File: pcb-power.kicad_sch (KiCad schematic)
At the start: 9 parts, among them Q1 PMOS, Q3 PMOS, Q4 PMOS, U1 LM1117MP-3.3, U2 LM1117MP-3.3

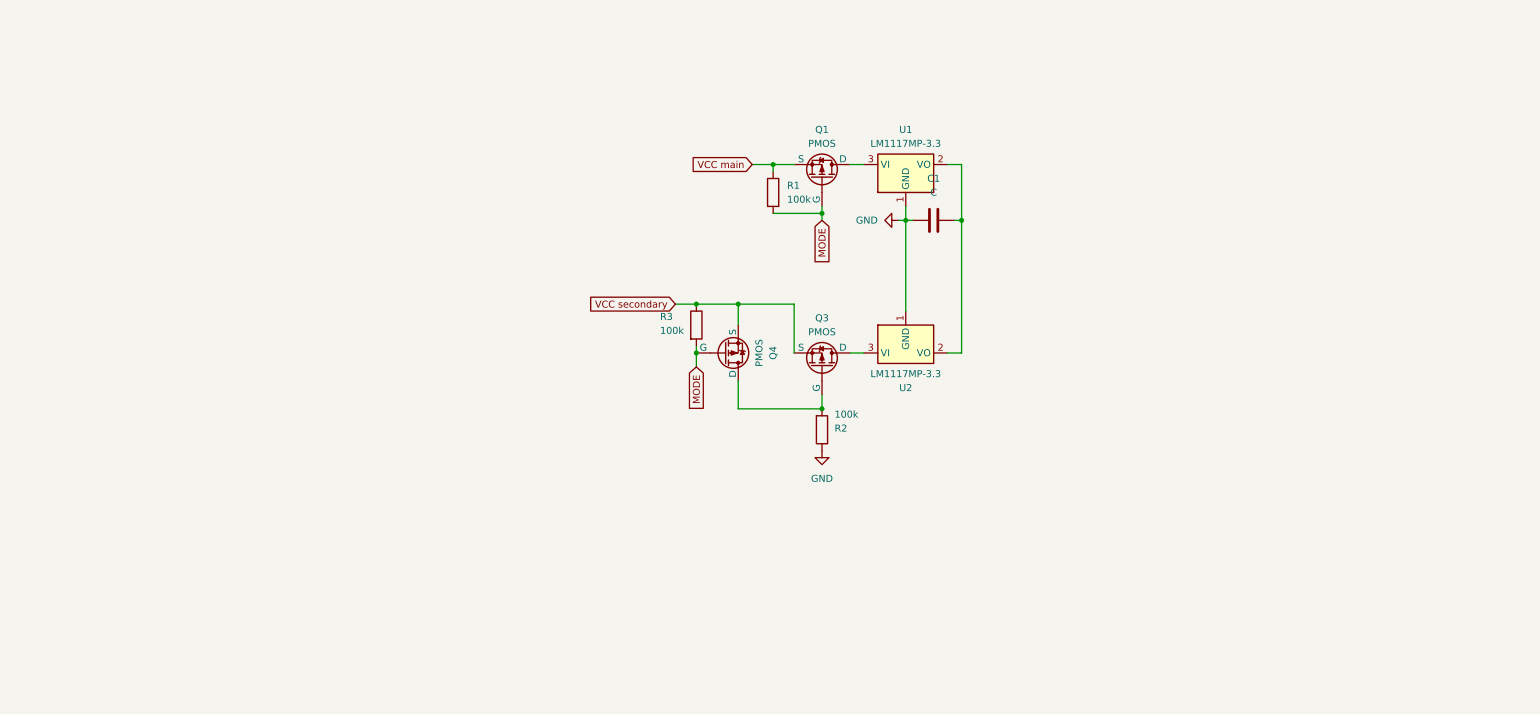
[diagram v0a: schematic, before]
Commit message: added pyro, voltage probes, signal
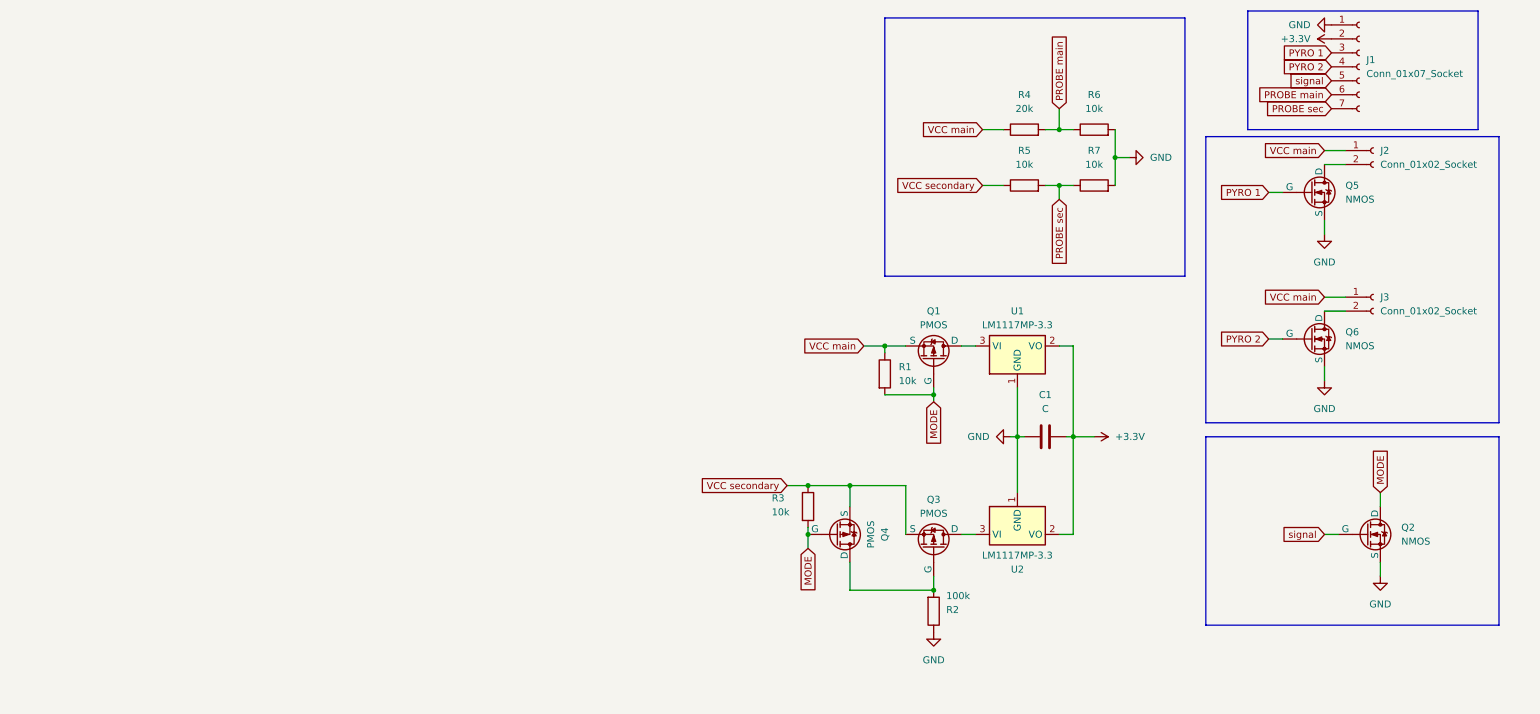
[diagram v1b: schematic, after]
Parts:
- added J1: Conn_01x07_Socket, symbol Connector:Conn_01x07_Socket
- added J2, J3: Conn_01x02_Socket, symbol Connector:Conn_01x02_Socket
- added Q2, Q5, Q6: NMOS, symbol Simulation_SPICE:NMOS
- added R4: 20k, symbol Device:R
- added R5, R6, R7: 10k, symbol Device:R
- R1, R3: value 100k -> 10k
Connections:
- net GND: now also J1.1 (Pin_1), Q2.3 (S), Q5.3 (S), Q6.3 (S), R6.2, R7.2
- net MODE: now also Q2.1 (D)
- net VCC main: now also J2.1 (Pin_1), J3.1 (Pin_1), R4.1
- net VCC secondary: now also R5.1
- net +3.3V: now reaches C1.2, U1.2 (VO), U2.2 (VO)
- net +3.3V: now also J1.2 (Pin_2)
- new net: J2.2 (Pin_2), Q5.1 (D)
- new net: J3.2 (Pin_2), Q6.1 (D)
- new net PROBE main: J1.6 (Pin_6), R4.2, R6.1
- new net PROBE sec: J1.7 (Pin_7), R5.2, R7.1
- new net PYRO 1: J1.3 (Pin_3), Q5.2 (G)
- new net PYRO 2: J1.4 (Pin_4), Q6.2 (G)
- new net signal: J1.5 (Pin_5), Q2.2 (G)
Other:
- moved on the sheet: C1, Q1, Q3, Q4, R1, R2, R3, U1, U2

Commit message: pcb design done
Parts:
- removed Q1, Q3: PMOS, symbol Simulation_SPICE:PMOS
- removed Q5, Q6: NMOS, symbol Simulation_SPICE:NMOS
- removed R1, R3: 10k, symbol Device:R
- removed R2: 100k, symbol Device:R
- removed U1, U2: LM1117MP-3.3, Package_TO_SOT_SMD:SOT-223-3_TabPin2, symbol Regulator_Linear:LM1117MP-3.3
- added R10, R8, R9: 10k, Resistor_THT:R_Axial_DIN0207_L6.3mm_D2.5mm_P10.16mm_Horizontal, symbol Device:R
- added U1, U3: LM1117DT-5.0, Package_TO_SOT_SMD:TO-252-3_TabPin2, symbol Regulator_Linear:LM1117DT-5.0
- added U2: IRF7303, Package_TO_SOT_SMD:IRF7303, symbol Transistor_FET:IRF7303
- added U4: IRF7104, Package_TO_SOT_SMD:IRF7104, symbol Transistor_FET:IRF7104
- C1: footprint (none) -> Capacitor_THT:CP_Radial_D5.0mm_P2.00mm
- J1: footprint (none) -> Connector_PinSocket_2.54mm:PinSocket_1x07_P2.54mm_Vertical
- J2, J3: footprint (none) -> ark:TerminalBlock_bornier-2_P5.08mm
- Q2: footprint (none) -> Package_TO_SOT_SMD:SOT-23
- Q4: footprint (none) -> Package_TO_SOT_SMD:TO-252-2
- R4, R5, R6, R7: footprint (none) -> Resistor_THT:R_Axial_DIN0207_L6.3mm_D2.5mm_P10.16mm_Horizontal
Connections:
- net +3.3V: now also U1.2 (VO), U3.2 (VO)
- net GND: now also R9.1, U1.1 (GND), U2.1 (S1), U2.3 (S2), U3.1 (GND)
- net MODE: now also R10.2, R8.1, U4.4 (G2)
- net PYRO 1: now also U2.2 (G1)
- net PYRO 2: now also U2.4 (G2)
- net VCC main: now also J2.2 (Pin_2), J3.2 (Pin_2), Q4.3 (S), R10.1, U4.1 (S1); no longer J2.1 (Pin_1), J3.1 (Pin_1)
- net VCC secondary: now also R8.2, U4.3 (S2); no longer Q4.3 (S)
- net at Q4.1 (D): now also R9.2, U4.2 (G1)
- new net: J2.1 (Pin_1), U2.5 (D2)
- new net: J3.1 (Pin_1), U2.6 (D1)
- new net: U3.3 (VI), U4.5 (D2)
- new net: U1.3 (VI), U4.6 (D1)
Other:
- moved on the sheet: C1, J2, J3, Q2

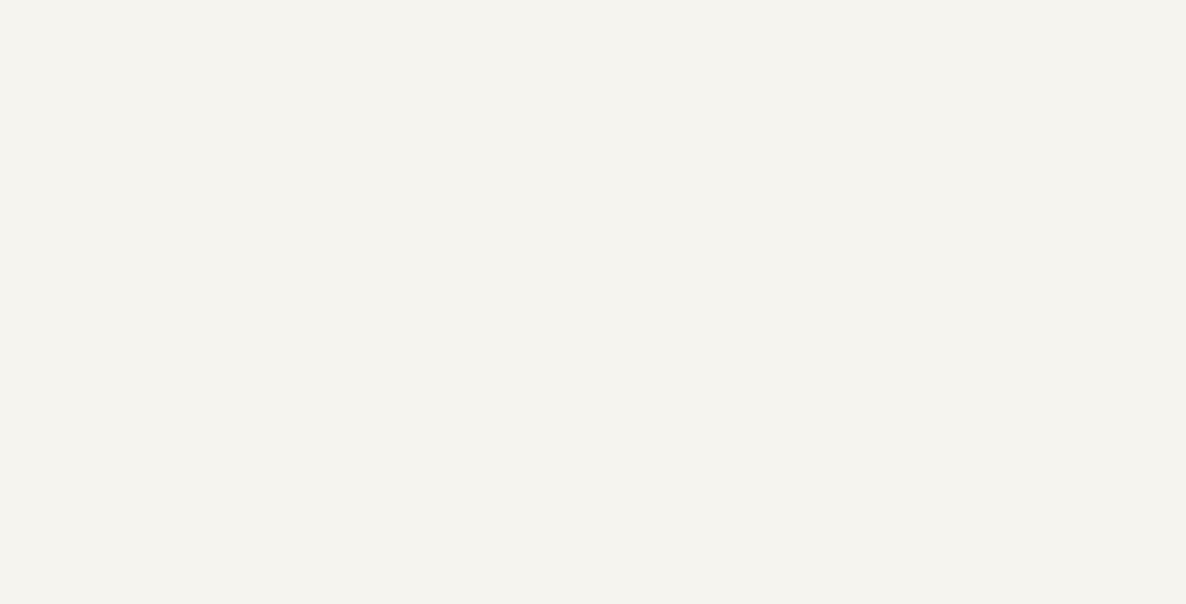
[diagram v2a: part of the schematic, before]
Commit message: added second layer for connecting batteries
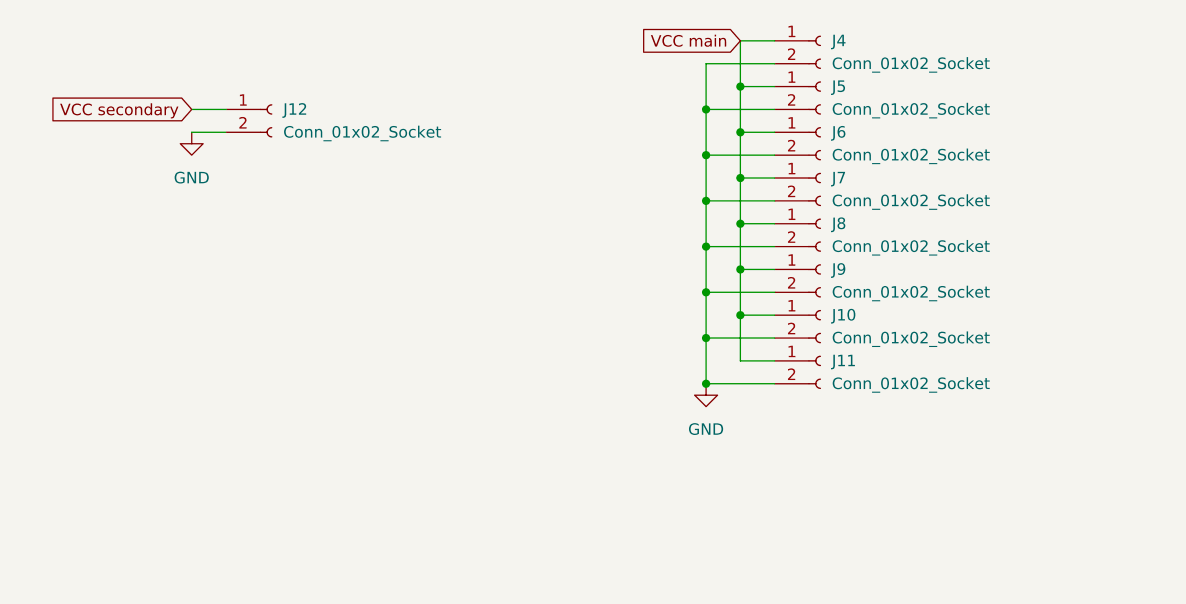
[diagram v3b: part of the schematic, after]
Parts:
- added J10, J11, J12, J4, J5, J6, J7, J8, J9: Conn_01x02_Socket, Connector_PinSocket_2.54mm:PinSocket_1x02_P2.54mm_Vertical, symbol Connector:Conn_01x02_Socket
- U1, U3: footprint Package_TO_SOT_SMD:TO-252-3_TabPin2 -> Package_TO_SOT_SMD:SOT-223
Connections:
- net GND: now also J10.2 (Pin_2), J11.2 (Pin_2), J12.2 (Pin_2), J4.2 (Pin_2), J5.2 (Pin_2), J6.2 (Pin_2), J7.2 (Pin_2), J8.2 (Pin_2), J9.2 (Pin_2)
- net VCC main: now also J10.1 (Pin_1), J11.1 (Pin_1), J4.1 (Pin_1), J5.1 (Pin_1), J6.1 (Pin_1), J7.1 (Pin_1), J8.1 (Pin_1), J9.1 (Pin_1)
- net VCC secondary: now also J12.1 (Pin_1)

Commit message: changed Vreg
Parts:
- U1, U3: footprint Package_TO_SOT_SMD:SOT-223 -> Package_TO_SOT_SMD:TO-252-2
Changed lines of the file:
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@@
 			)
 		)
-		(property "Footprint" "Package_TO_SOT_SMD:SOT-223"
+		(property "Footprint" "Package_TO_SOT_SMD:TO-252-2"
 			(at 196.85 93.98 0)
 			(effects
@@
 			)
 		)
-		(property "Footprint" "Package_TO_SOT_SMD:SOT-223"
+		(property "Footprint" "Package_TO_SOT_SMD:TO-252-2"
 			(at 196.85 128.27 0)
 			(effects

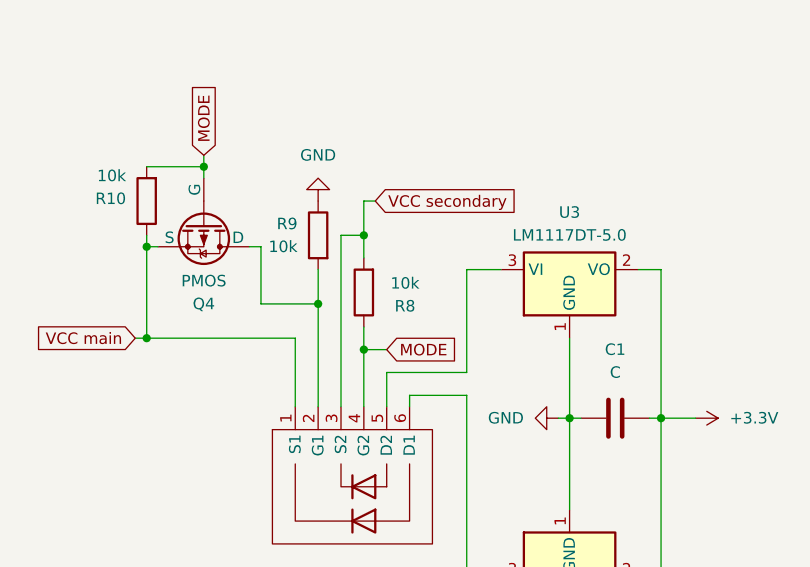
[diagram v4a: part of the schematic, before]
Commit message: changed resistor value
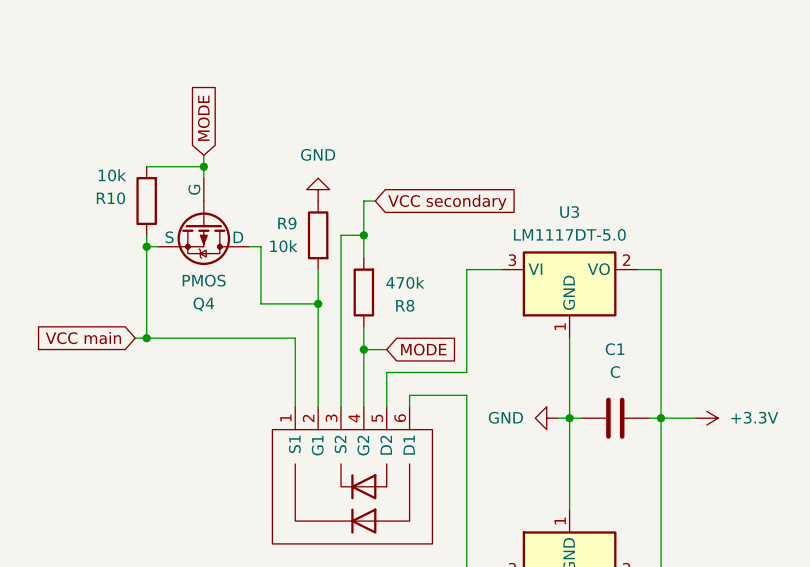
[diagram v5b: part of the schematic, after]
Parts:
- R8: value 10k -> 470k
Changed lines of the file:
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@@
 			)
 		)
-		(property "Value" "10k"
+		(property "Value" "470k"
 			(at 178.562 95.504 0)
 			(effects
